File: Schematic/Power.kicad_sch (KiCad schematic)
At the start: 41 parts, among them IC1 MP9943AGQ-Z, IC2 MP9943AGQ-Z, U2 ME6217C33M5G, U3 LDO-1.8v

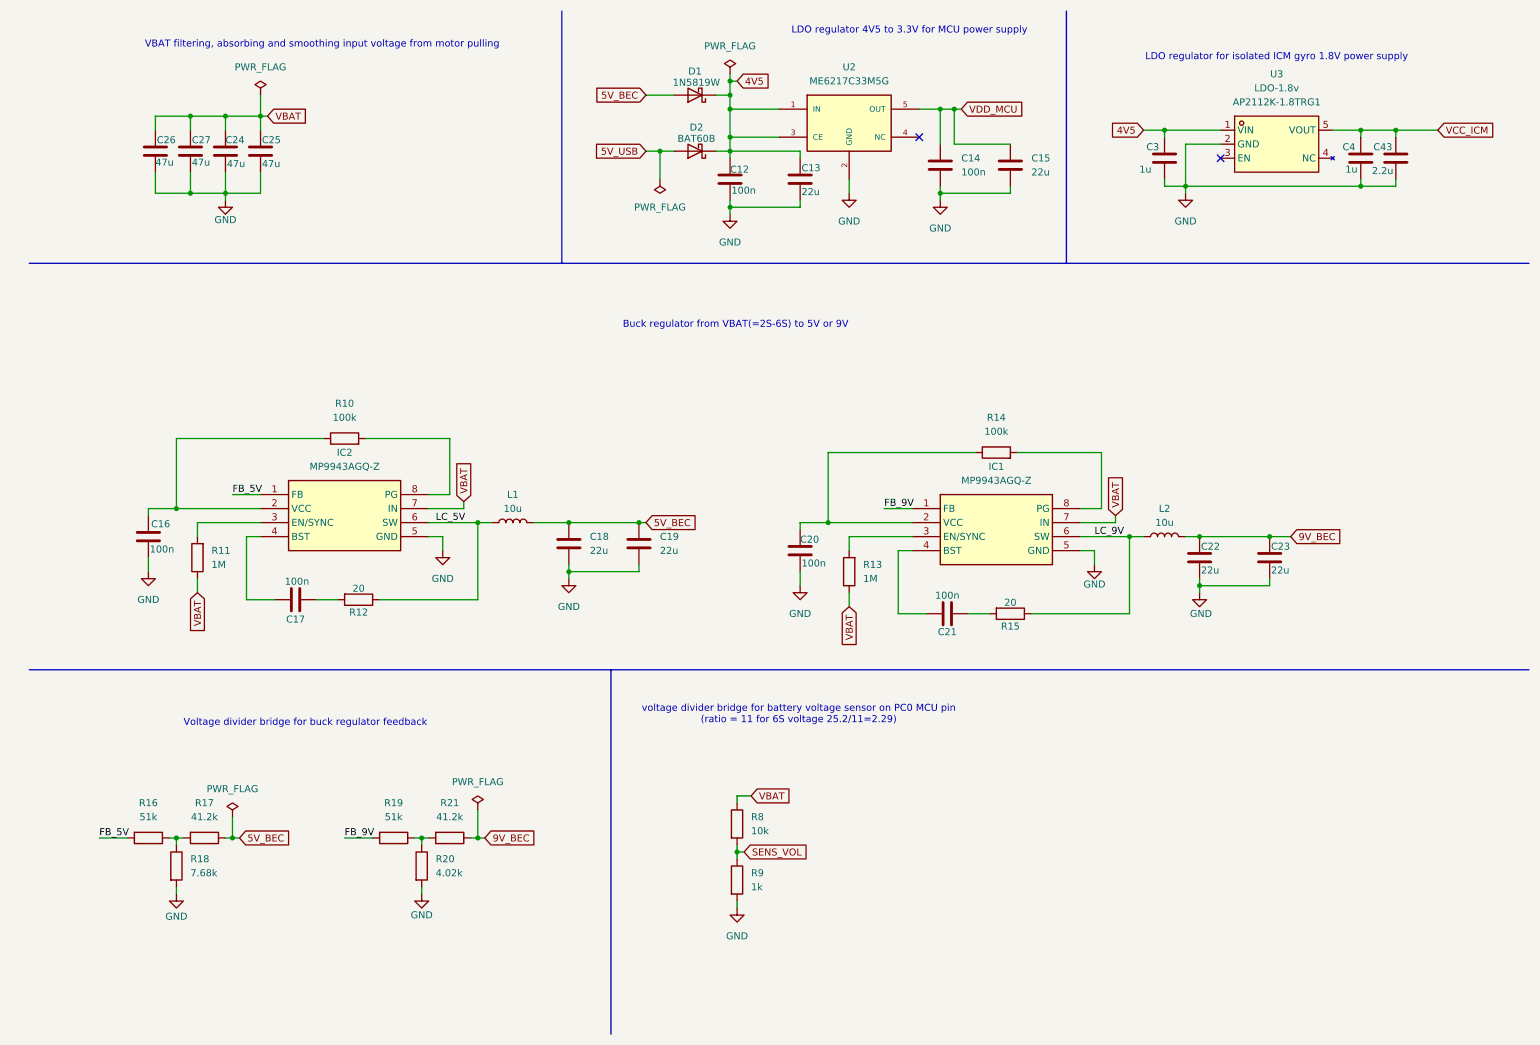
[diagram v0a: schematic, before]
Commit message: optimisation : - refactoring two 4 pin connector for mag and gps into one 6 pin connector - increased output voltage from 5V buck regulator to take into account voltage decrease schottky diodes
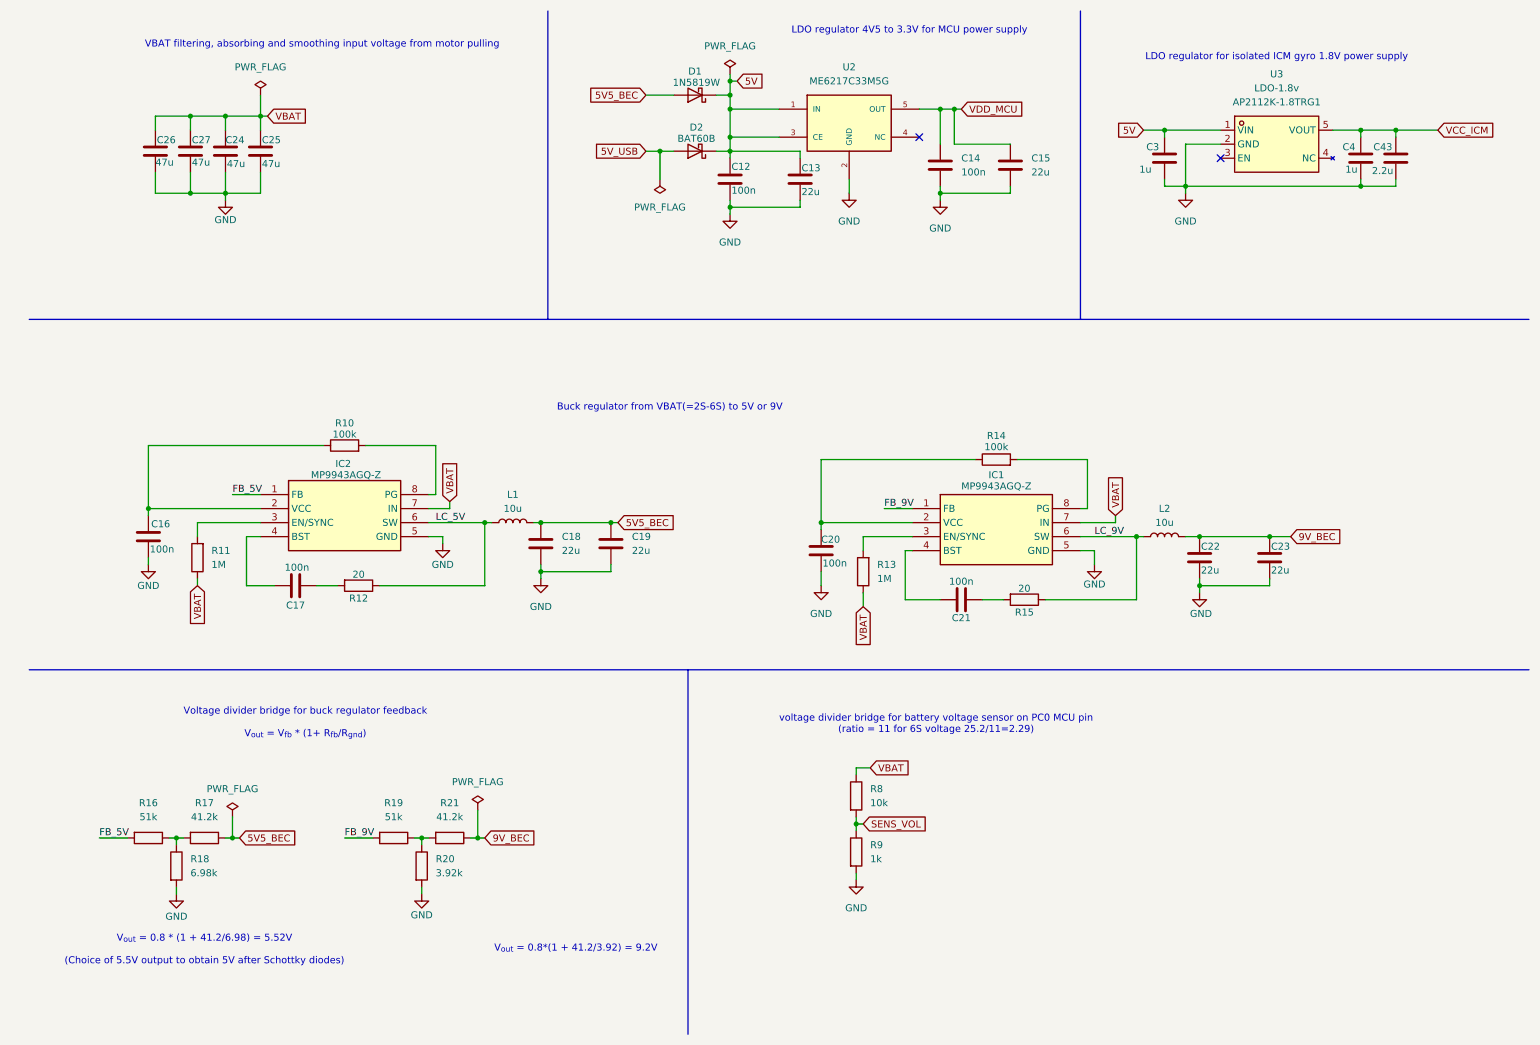
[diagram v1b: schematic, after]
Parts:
- R18: value 7.68k -> 6.98k; MPN RS-03K7681FT -> ERA-3AEB6981V; Manufacturer FH -> Panasonic
- R20: value 4.02k -> 3.92k; MPN 0603WAF4021T5E -> ERA-3ARB3921V; Manufacturer UNI-ROYAL -> Panasonic
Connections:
- net 4V5 renamed 5V
- net 5V_BEC renamed 5V5_BEC
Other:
- note added: "V_{out} = 0.8 * (1 + 41.2/6.98) = 5.52V (Choice of 5.5V output to obtain 5V after Schottky diodes)"
- note added: "V_{out} = 0.8*(1 + 41.2/3.92) = 9.2V"
- note added: "Voltage divider bridge for buck regulator feedback V_{out} = V_{fb} * (1+ R_{fb}/R_{gnd})"
- note removed: "Voltage divider bridge for buck regulator feedback"
- moved on the sheet: C17, C18, C19, C20, C21, R10, R12, R13, R14, R15, R8, R9

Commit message: update routing
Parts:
- C12, C14, C16, C17, C20, C21, C3, C4, C43: footprint Capacitor_SMD:C_0603_1608Metric -> Capacitor_SMD:C_0402_1005Metric
- C13, C15, C18, C19, C22, C23: footprint Capacitor_SMD:C_0805_2012Metric -> Capacitor_SMD:C_0402_1005Metric
- C24, C25, C26, C27: footprint Capacitor_SMD:C_1206_3216Metric -> Capacitor_SMD:C_0603_1608Metric
- R10, R11, R12, R13, R14, R15, R16, R17, R18, R19, R20, R21, R8, R9: footprint Resistor_SMD:R_0603_1608Metric -> Capacitor_SMD:C_0402_1005Metric
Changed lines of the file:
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@@
 			)
 		)
-		(property "Footprint" "Capacitor_SMD:C_0603_1608Metric"
+		(property "Footprint" "Capacitor_SMD:C_0402_1005Metric"
 			(at 254.9652 43.18 0)
 			(effects
@@
 			)
 		)
-		(property "Footprint" "Resistor_SMD:R_0603_1608Metric"
+		(property "Footprint" "Capacitor_SMD:C_0402_1005Metric"
 			(at 82.042 167.64 90)
 			(effects
@@
 			)
 		)
-		(property "Footprint" "Capacitor_SMD:C_0603_1608Metric"
+		(property "Footprint" "Capacitor_SMD:C_0402_1005Metric"
 			(at 219.4052 43.18 0)
 			(effects
@@
 			)
 		)
-		(property "Footprint" "Capacitor_SMD:C_1206_3216Metric"
+		(property "Footprint" "Capacitor_SMD:C_0603_1608Metric"
 			(at 42.8752 41.91 0)
 			(effects
@@
 			)
 		)
-		(property "Footprint" "Capacitor_SMD:C_1206_3216Metric"
+		(property "Footprint" "Capacitor_SMD:C_0603_1608Metric"
 			(at 36.5252 41.91 0)
 			(effects
@@
 			)
 		)
-		(property "Footprint" "Capacitor_SMD:C_0805_2012Metric"
+		(property "Footprint" "Capacitor_SMD:C_0402_1005Metric"
 			(at 106.3752 113.03 0)
 			(effects
@@
 			)
 		)
-		(property "Footprint" "Capacitor_SMD:C_0603_1608Metric"
+		(property "Footprint" "Capacitor_SMD:C_0402_1005Metric"
 			(at 178.7652 44.45 0)
 			(effects
@@
 			)
 		)
-		(property "Footprint" "Resistor_SMD:R_0603_1608Metric"
+		(property "Footprint" "Capacitor_SMD:C_0402_1005Metric"
 			(at 187.96 95.758 90)
 			(effects
@@
 			)
 		)
-		(property "Footprint" "Resistor_SMD:R_0603_1608Metric"
+		(property "Footprint" "Capacitor_SMD:C_0402_1005Metric"
 			(at 193.04 117.602 90)
 			(effects
@@
 			)
 		)
-		(property "Footprint" "Resistor_SMD:R_0603_1608Metric"
+		(property "Footprint" "Capacitor_SMD:C_0402_1005Metric"
 			(at 88.9 160.782 90)
 			(effects
@@
 			)
 		)
-		(property "Footprint" "Resistor_SMD:R_0603_1608Metric"
+		(property "Footprint" "Capacitor_SMD:C_0402_1005Metric"
 			(at 72.39 115.062 90)
 			(effects
@@
 			)
 		)
-		(property "Footprint" "Capacitor_SMD:C_0603_1608Metric"
+		(property "Footprint" "Capacitor_SMD:C_0402_1005Metric"
 			(at 177.8 120.3452 0)
 			(effects
@@
 			)
 		)
-		(property "Footprint" "Capacitor_SMD:C_0603_1608Metric"
+		(property "Footprint" "Capacitor_SMD:C_0402_1005Metric"
 			(at 261.3152 43.18 0)
 			(effects
@@
 			)
 		)
-		(property "Footprint" "Resistor_SMD:R_0603_1608Metric"
+		(property "Footprint" "Capacitor_SMD:C_0402_1005Metric"
 			(at 69.85 93.218 90)
 			(effects
@@
 			)
 		)
-		(property "Footprint" "Capacitor_SMD:C_0603_1608Metric"
+		(property "Footprint" "Capacitor_SMD:C_0402_1005Metric"
 			(at 140.6652 46.99 0)
 			(effects
@@
 			)
 		)
-		(property "Footprint" "Resistor_SMD:R_0603_1608Metric"
+		(property "Footprint" "Capacitor_SMD:C_0402_1005Metric"
 			(at 78.74 160.782 90)
 			(effects
@@
 			)
 		)
-		(property "Footprint" "Resistor_SMD:R_0603_1608Metric"
+		(property "Footprint" "Capacitor_SMD:C_0402_1005Metric"
 			(at 44.45 160.782 90)
 			(effects
@@
 			)
 		)
-		(property "Footprint" "Capacitor_SMD:C_0603_1608Metric"
+		(property "Footprint" "Capacitor_SMD:C_0402_1005Metric"
 			(at 155.2448 106.68 0)
 			(effects
@@
 			)
 		)
-		(property "Footprint" "Capacitor_SMD:C_0805_2012Metric"
+		(property "Footprint" "Capacitor_SMD:C_0402_1005Metric"
 			(at 238.4552 115.57 0)
 			(effects
@@
 			)
 		)
-		(property "Footprint" "Capacitor_SMD:C_0805_2012Metric"
+		(property "Footprint" "Capacitor_SMD:C_0402_1005Metric"
 			(at 153.3652 46.99 0)
 			(effects
@@
 			)
 		)
-		(property "Footprint" "Capacitor_SMD:C_0805_2012Metric"
+		(property "Footprint" "Capacitor_SMD:C_0402_1005Metric"
 			(at 191.4652 44.45 0)
 			(effects
@@
 			)
 		)
-		(property "Footprint" "Resistor_SMD:R_0603_1608Metric"
+		(property "Footprint" "Capacitor_SMD:C_0402_1005Metric"
 			(at 44.958 111.76 90)
 			(effects
@@
 			)
 		)
-		(property "Footprint" "Resistor_SMD:R_0603_1608Metric"
+		(property "Footprint" "Capacitor_SMD:C_0402_1005Metric"
 			(at 37.592 167.64 90)
 			(effects
@@
 			)
 		)
-		(property "Footprint" "Capacitor_SMD:C_1206_3216Metric"
+		(property "Footprint" "Capacitor_SMD:C_0603_1608Metric"
 			(at 55.5752 41.91 0)
 			(effects
@@
 			)
 		)
-		(property "Footprint" "Capacitor_SMD:C_0603_1608Metric"
+		(property "Footprint" "Capacitor_SMD:C_0402_1005Metric"
 			(at 57.15 117.8052 0)
 			(effects
@@
 			)
 		)
-		(property "Footprint" "Resistor_SMD:R_0603_1608Metric"
+		(property "Footprint" "Capacitor_SMD:C_0402_1005Metric"
 			(at 160.782 154.94 90)
 			(effects
@@
 			)
 		)
-		(property "Footprint" "Resistor_SMD:R_0603_1608Metric"
+		(property "Footprint" "Capacitor_SMD:C_0402_1005Metric"
 			(at 34.29 160.782 90)
 			(effects
@@
 			)
 		)
-		(property "Footprint" "Capacitor_SMD:C_0805_2012Metric"
+		(property "Footprint" "Capacitor_SMD:C_0402_1005Metric"
 			(at 119.0752 113.03 0)
 			(effects
@@
 			)
 		)
-		(property "Footprint" "Resistor_SMD:R_0603_1608Metric"
+		(property "Footprint" "Capacitor_SMD:C_0402_1005Metric"
 			(at 160.782 165.1 90)
 			(effects
@@
 			)
 		)
-		(property "Footprint" "Capacitor_SMD:C_0805_2012Metric"
+		(property "Footprint" "Capacitor_SMD:C_0402_1005Metric"
 			(at 225.7552 115.57 0)
 			(effects
@@
 			)
 		)
-		(property "Footprint" "Resistor_SMD:R_0603_1608Metric"
+		(property "Footprint" "Capacitor_SMD:C_0402_1005Metric"
 			(at 165.608 114.3 90)
 			(effects
@@
 			)
 		)
-		(property "Footprint" "Capacitor_SMD:C_0603_1608Metric"
+		(property "Footprint" "Capacitor_SMD:C_0402_1005Metric"
 			(at 33.3248 104.14 0)
 			(effects
@@
 			)
 		)
-		(property "Footprint" "Capacitor_SMD:C_1206_3216Metric"
+		(property "Footprint" "Capacitor_SMD:C_0603_1608Metric"
 			(at 49.2252 41.91 0)
 			(effects

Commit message: update routing
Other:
- note added: "LDO regulator 5V to 3.3V for MCU power supply"
- note removed: "LDO regulator 4V5 to 3.3V for MCU power supply"
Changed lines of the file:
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@@
 		)
 	)
-	(text "LDO regulator 4V5 to 3.3V for MCU power supply"
+	(text "LDO regulator 5V to 3.3V for MCU power supply"
 		(exclude_from_sim no)
 		(at 172.212 16.256 0)

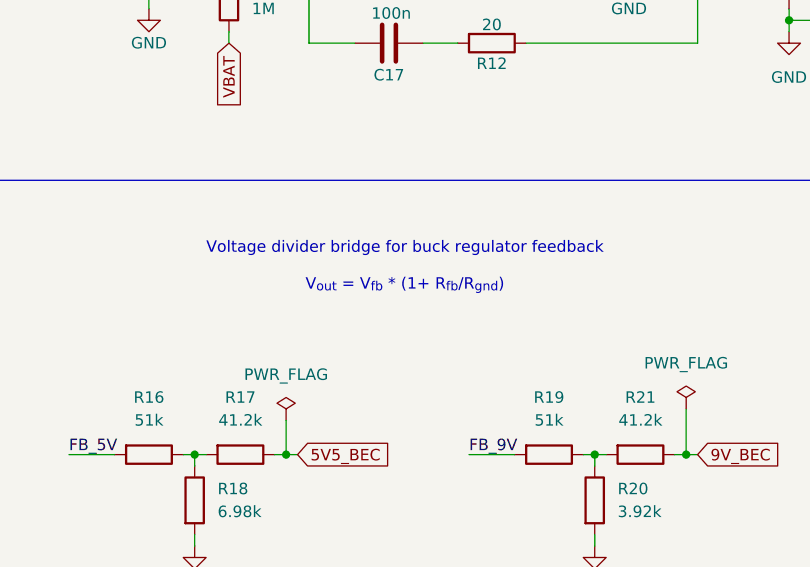
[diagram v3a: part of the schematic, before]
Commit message: fix: update voltage divider formula in Power schematic; remove unused project files
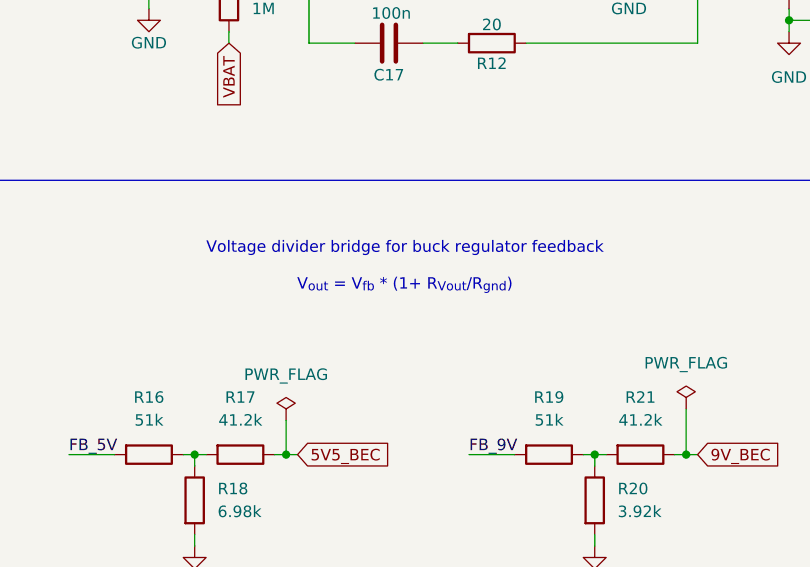
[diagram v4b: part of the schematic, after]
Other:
- note added: "Voltage divider bridge for buck regulator feedback V_{out} = V_{fb} * (1+ R_{Vout}/R_{gnd})"
- note removed: "Voltage divider bridge for buck regulator feedback V_{out} = V_{fb} * (1+ R_{fb}/R_{gnd})"
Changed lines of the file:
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@@
 		)
 	)
-	(text "Voltage divider bridge for buck regulator feedback\n\nV_{out} = V_{fb} * (1+ R_{fb}/R_{gnd})"
+	(text "Voltage divider bridge for buck regulator feedback\n\nV_{out} = V_{fb} * (1+ R_{Vout}/R_{gnd})"
 		(exclude_from_sim no)
 		(at 62.738 141.732 0)
